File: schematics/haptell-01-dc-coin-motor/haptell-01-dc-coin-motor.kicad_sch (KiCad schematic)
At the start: 5 parts, among them M1 3-5V DC coin motor, Q1 IRF3205

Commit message: Improve KiCad motor driver schematic
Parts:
- removed D1: 1N5819, symbol Device:D_Schottky
- removed M1: 3-5V DC coin motor, symbol Motor:Motor_DC
- removed Q1: IRF3205, symbol Transistor_FET:IRF3205
- removed R1: 220R, symbol Device:R
- removed R2: 10k, symbol Device:R
- added D1: 1N5819, symbol D_Schottky
- added M1: 3-5V DC coin motor, symbol Motor_DC
- added Q1: IRF3205, Package_TO_SOT_THT:TO-220-3_Vertical, symbol Q_NMOS
- added R1: 220R, symbol R
- added R2: 10k, symbol R
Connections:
- net GND: now also Q1.S, R2.2
- new net: Q1.G, R2.1
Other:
- note added: "Arduino UNO R4 WiFi pins"
- note added: "D1 flyback diode: cathode / marked end to +5V, anode to drain node."
- note added: "D9 PWM drives only the MOSFET gate. Motor current flows through Q1."
- note added: "Motor driver stage"
- note added: "common ground"
- note added: "drain node: motor - / diode anode / Q1 drain"
- note added: "gate pulldown"
- note added: "haptell-01 DC coin vibration motor driver"
- note removed: "Arduino UNO R4 WiFi connections: D9 PWM -> R1 -> MOSFET gate 5V -> motor positive GND -> MOSFET source and pulldown"
- note removed: "D1 cathode / marked end to 5V. D1 anode to MOSFET drain."
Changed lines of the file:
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@@
     (title "haptell-01 DC Coin Motor Driver")
     (date "2026-05-12")
-    (rev "0.1")
+    (rev "0.2")
     (company "Haptell")
     (comment 1 "Arduino UNO R4 WiFi low-side MOSFET motor driver")
   )
-  (junction (at 88.9 58.42) (diameter 0) (color 0 0 0 0)
+  (text "haptell-01 DC coin vibration motor driver" (at 25.4 25.4 0)
+    (effects (font (size 3.048 3.048) (bold yes)) (justify left bottom))
   )
-  (junction (at 88.9 109.22) (diameter 0) (color 0 0 0 0)
+  (text "D9 PWM drives only the MOSFET gate. Motor current flows through Q1." (at 25.4 31.75 0)
+    (effects (font (size 1.778 1.778)) (justify left bottom))
   )
-  (junction (at 139.7 76.2) (diameter 0) (color 0 0 0 0)
+  (text "D1 flyback diode: cathode / marked end to +5V, anode to drain node." (at 25.4 36.83 0)
+    (effects (font (size 1.778 1.778)) (justify left bottom))
   )
-  (wire (pts (xy 25.4 58.42) (xy 45.72 58.42))
-    (stroke (width 0) (type default))
+  (text "Arduino UNO R4 WiFi pins" (at 25.4 43.18 0)
+    (effects (font (size 1.778 1.778) (bold yes)) (justify left bottom))
   )
-  (wire (pts (xy 66.04 58.42) (xy 88.9 58.42))
-    (stroke (width 0) (type default))
+  (text "Motor driver stage" (at 101.6 43.18 0)
+    (effects (font (size 1.778 1.778) (bold yes)) (justify left bottom))
   )
-  (wire (pts (xy 88.9 58.42) (xy 88.9 76.2))
-    (stroke (width 0) (type default))
-  )
-  (wire (pts (xy 88.9 58.42) (xy 114.3 58.42))
-    (stroke (width 0) (type default))
-  )
-  (wire (pts (xy 25.4 76.2) (xy 114.3 76.2))
-    (stroke (width 0) (type default))
-  )
-  (wire (pts (xy 134.62 76.2) (xy 139.7 76.2))
-    (stroke (width 0) (type default))
-  )
-  (wire (pts (xy 139.7 76.2) (xy 139.7 88.9))
-    (stroke (width 0) (type default))
-  )
-  (wire (pts (xy 139.7 76.2) (xy 157.48 76.2))
-    (stroke (width 0) (type default))
-  )
-  (wire (pts (xy 88.9 96.52) (xy 88.9 109.22))
-    (stroke (width 0) (type default))
-  )
-  (wire (pts (xy 25.4 109.22) (xy 88.9 109.22))
-    (stroke (width 0) (type default))
-  )
-  (wire (pts (xy 88.9 109.22) (xy 139.7 109.22))
-    (stroke (width 0) (type default))
-  )
-  (wire (pts (xy 139.7 99.06) (xy 139.7 109.22))
-    (stroke (width 0) (type default))
-  )
-  (text "Arduino UNO R4 WiFi connections:\nD9 PWM -> R1 -> MOSFET gate\n5V -> motor positive\nGND -> MOSFET source and pulldown" (at 24.13 30.48 0)
-    (effects (font (size 3.048 3.048)) (justify left bottom))
-  )
-  (text "D1 cathode / marked end to 5V.\nD1 anode to MOSFET drain." (at 104.14 43.18 0)
-    (effects (font (size 2.54 2.54)) (justify left bottom))
-  )
-  (global_label "D9_PWM" (shape input) (at 25.4 58.42 180)
+  (global_label "D9_PWM" (shape input) (at 25.4 88.9 180)
     (effects (font (size 1.27 1.27)) (justify right))
   )
-  (global_label "+5V" (shape passive) (at 25.4 76.2 180)
+  (global_label "+5V" (shape passive) (at 25.4 55.88 180)
     (effects (font (size 1.27 1.27)) (justify right))
   )
-  (global_label "GND" (shape passive) (at 25.4 109.22 180)
+  (global_label "GND" (shape passive) (at 25.4 127 180)
     (effects (font (size 1.27 1.27)) (justify right))
   )
-  (symbol (lib_id "Device:R") (at 55.88 58.42 90) (unit 1)
+  (junction (at 81.28 88.9) (diameter 0) (color 0 0 0 0))
+  (junction (at 81.28 127) (diameter 0) (color 0 0 0 0))
+  (junction (at 111.76 55.88) (diameter 0) (color 0 0 0 0))
+  (junction (at 139.7 78.74) (diameter 0) (color 0 0 0 0))
+  (junction (at 142.24 127) (diameter 0) (color 0 0 0 0))
+  (wire (pts (xy 25.4 88.9) (xy 48.26 88.9)) (stroke (width 0) (type default)))
+  (wire (pts (xy 58.42 88.9) (xy 81.28 88.9)) (stroke (width 0) (type default)))
+  (wire (pts (xy 81.28 88.9) (xy 99.06 88.9)) (stroke (width 0) (type default)))
+  (wire (pts (xy 99.06 88.9) (xy 99.06 109.22)) (stroke (width 0) (type default)))
+  (wire (pts (xy 99.06 109.22) (xy 134.62 109.22)) (stroke (width 0) (type default)))
+  (wire (pts (xy 81.28 88.9) (xy 81.28 101.6)) (stroke (width 0) (type default)))
+  (wire (pts (xy 81.28 109.22) (xy 81.28 127)) (stroke (width 0) (type default)))
+  (wire (pts (xy 25.4 55.88) (xy 111.76 55.88)) (stroke (width 0) (type default)))
+  (wire (pts (xy 111.76 55.88) (xy 124.46 55.88)) (stroke (width 0) (type default)))
+  (wire (pts (xy 111.76 55.88) (xy 111.76 68.58)) (stroke (width 0) (type default)))
+  (wire (pts (xy 111.76 68.58) (xy 124.46 68.58)) (stroke (width 0) (type default)))
+  (wire (pts (xy 124.46 78.74) (xy 139.7 78.74)) (stroke (width 0) (type default)))
+  (wire (pts (xy 139.7 78.74) (xy 142.24 78.74)) (stroke (width 0) (type default)))
+  (wire (pts (xy 142.24 78.74) (xy 142.24 104.14)) (stroke (width 0) (type default)))
+  (wire (pts (xy 142.24 114.3) (xy 142.24 127)) (stroke (width 0) (type default)))
+  (wire (pts (xy 142.24 127) (xy 25.4 127)) (stroke (width 0) (type default)))
+  (text "gate pulldown" (at 64.77 112.395 0)
+    (effects (font (size 1.27 1.27)) (justify left bottom))
+  )
+  (text "drain node: motor - / diode anode / Q1 drain" (at 142.24 80.01 0)
+    (effects (font (size 1.27 1.27)) (justify left bottom))
+  )
+  (text "common ground" (at 142.24 127 0)
+    (effects (font (size 1.27 1.27)) (justify left bottom))
+  )
+  (symbol (lib_id "R") (at 53.34 88.9 90) (unit 1)
     (in_bom yes) (on_board yes)
-    (property "Reference" "R1" (at 55.88 53.34 90)
-      (effects (font (size 1.27 1.27)))
-    )
-    (property "Value" "220R" (at 55.88 63.5 90)
-      (effects (font (size 1.27 1.27)))
-    )
-    (property "Footprint" "" (at 55.88 58.42 0)
-      (effects (font (size 1.27 1.27)) hide)
-    )
+    (property "Reference" "R1" (at 53.34 83.82 90) (effects (font (size 1.27 1.27))))
+    (property "Value" "220R" (at 53.34 93.98 90) (effects (font (size 1.27 1.27))))
+    (property "Footprint" "" (at 53.34 88.9 0) (effects (font (size 1.27 1.27)) hide))
+    (property "Datasheet" "" (at 53.34 88.9 0) (effects (font (size 1.27 1.27)) hide))
     (pin "1")
     (pin "2")
   )
-  (symbol (lib_id "Device:R") (at 88.9 86.36 0) (unit 1)
+  (symbol (lib_id "R") (at 81.28 105.41 0) (unit 1)
     (in_bom yes) (on_board yes)
-    (property "Reference" "R2" (at 93.98 83.82 0)
-      (effects (font (size 1.27 1.27)))
-    )
-    (property "Value" "10k" (at 93.98 88.9 0)
-      (effects (font (size 1.27 1.27)))
-    )
-    (property "Footprint" "" (at 88.9 86.36 0)
-      (effects (font (size 1.27 1.27)) hide)
-    )
+    (property "Reference" "R2" (at 86.36 102.87 0) (effects (font (size 1.27 1.27))))
+    (property "Value" "10k" (at 86.36 107.95 0) (effects (font (size 1.27 1.27))))
+    (property "Footprint" "" (at 81.28 105.41 0) (effects (font (size 1.27 1.27)) hide))
+    (property "Datasheet" "" (at 81.28 105.41 0) (effects (font (size 1.27 1.27)) hide))
     (pin "1")
     (pin "2")
   )
-  (symbol (lib_id "Motor:Motor_DC") (at 124.46 76.2 90) (unit 1)
+  (symbol (lib_id "Motor_DC") (at 124.46 63.5 0) (unit 1)
     (in_bom yes) (on_board yes)
-    (property "Reference" "M1" (at 124.46 68.58 90)
-      (effects (font (size 1.27 1.27)))
-    )
-    (property "Value" "3-5V DC coin motor" (at 124.46 83.82 90)
-      (effects (font (size 1.27 1.27)))
-    )
-    (property "Footprint" "" (at 124.46 76.2 0)
-      (effects (font (size 1.27 1.27)) hide)
-    )
+    (property "Reference" "M1" (at 128.27 55.88 0) (effects (font (size 1.27 1.27))))
+    (property "Value" "3-5V DC coin motor" (at 128.27 71.12 0) (effects (font (size 1.27 1.27))))
+    (property "Footprint" "" (at 124.46 63.5 0) (effects (font (size 1.27 1.27)) hide))
+    (property "Datasheet" "" (at 124.46 63.5 0) (effects (font (size 1.27 1.27)) hide))
     (pin "1")
     (pin "2")
   )
-  (symbol (lib_id "Device:D_Schottky") (at 124.46 58.42 90) (unit 1)
+  (symbol (lib_id "D_Schottky") (at 111.76 73.66 90) (unit 1)
     (in_bom yes) (on_board yes)
-    (property "Reference" "D1" (at 124.46 50.8 90)
-      (effects (font (size 1.27 1.27)))
-    )
-    (property "Value" "1N5819" (at 124.46 66.04 90)
-      (effects (font (size 1.27 1.27)))
-    )
-    (property "Footprint" "" (at 124.46 58.42 0)
-      (effects (font (size 1.27 1.27)) hide)
-    )
+    (property "Reference" "D1" (at 106.68 73.66 90) (effects (font (size 1.27 1.27))))
+    (property "Value" "1N5819" (at 116.84 73.66 90) (effects (font (size 1.27 1.27))))
+    (property "Footprint" "" (at 111.76 73.66 0) (effects (font (size 1.27 1.27)) hide))
+    (property "Datasheet" "" (at 111.76 73.66 0) (effects (font (size 1.27 1.27)) hide))
     (pin "1")
     (pin "2")
   )
-  (symbol (lib_id "Transistor_FET:IRF3205") (at 139.7 93.98 0) (unit 1)
+  (symbol (lib_id "Q_NMOS") (at 139.7 109.22 0) (unit 1)
     (in_bom yes) (on_board yes)
-    (property "Reference" "Q1" (at 146.05 91.44 0)
-      (effects (font (size 1.27 1.27)))
-    )
-    (property "Value" "IRF3205" (at 147.32 96.52 0)
-      (effects (font (size 1.27 1.27)))
-    )
-    (property "Footprint" "" (at 144.78 101.6 0)
-      (effects (font (size 1.27 1.27)) hide)
-    )
+    (property "Reference" "Q1" (at 146.05 105.41 0) (effects (font (size 1.27 1.27))))
+    (property "Value" "IRF3205" (at 146.05 110.49 0) (effects (font (size 1.27 1.27))))
+    (property "Footprint" "Package_TO_SOT_THT:TO-220-3_Vertical" (at 144.78 111.76 0) (effects (font (size 1.27 1.27)) hide))
+    (property "Datasheet" "http://www.irf.com/product-info/datasheets/data/irf3205.pdf" (at 139.7 109.22 0) (effects (font (size 1.27 1.27)) hide))
     (pin "G")
     (pin "D")

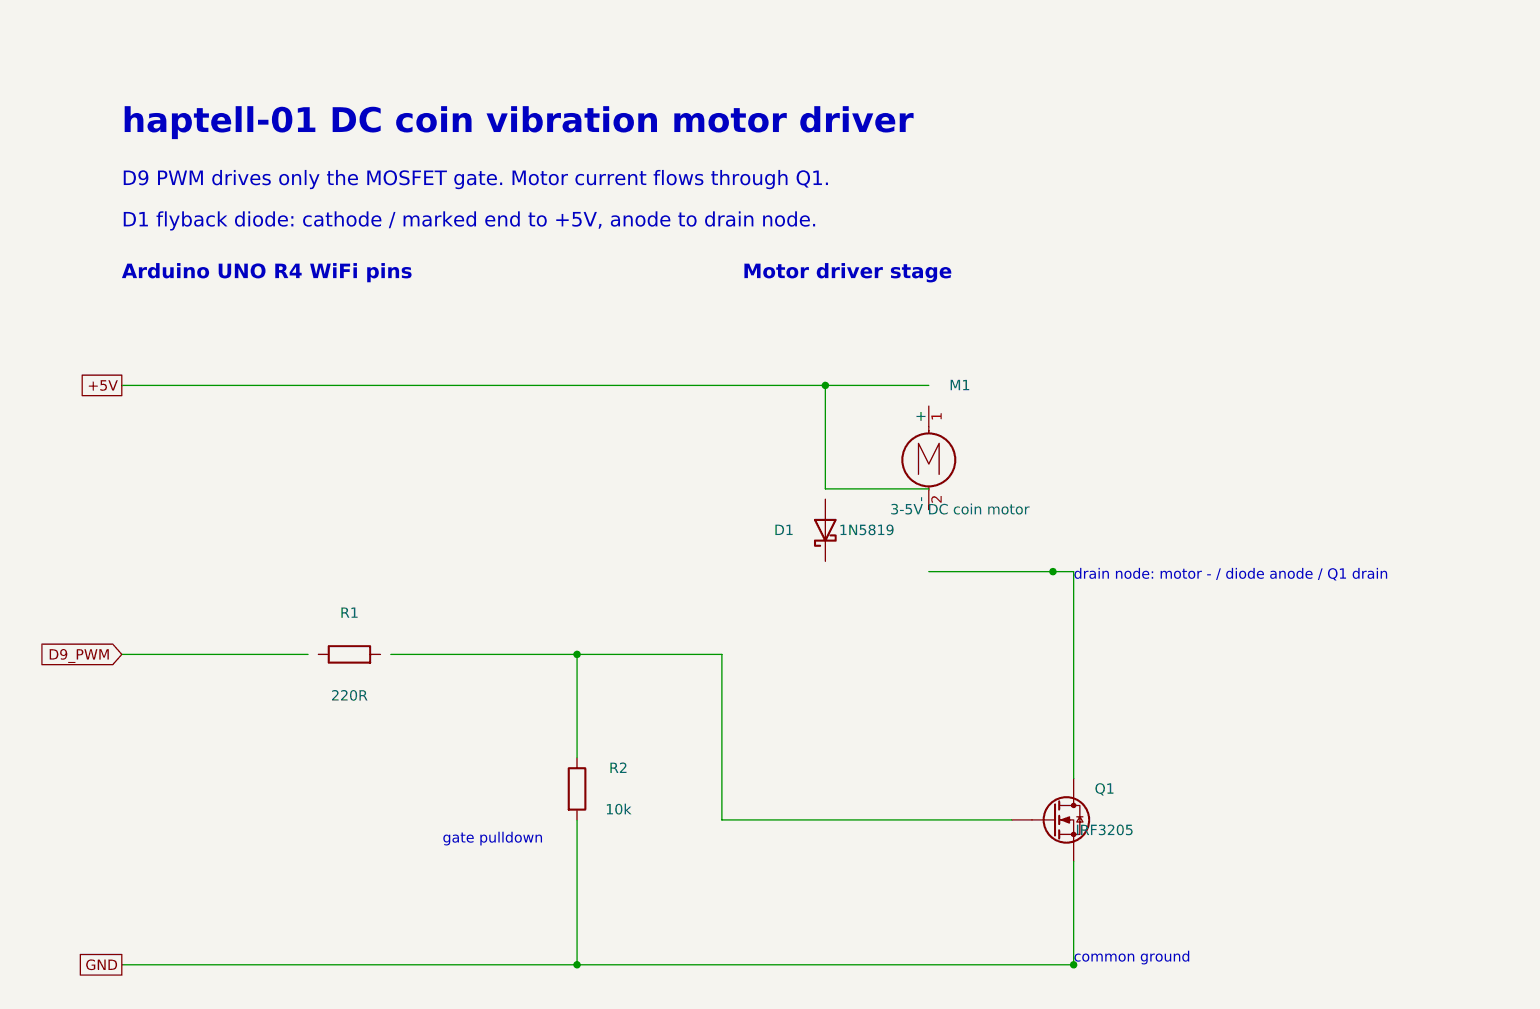
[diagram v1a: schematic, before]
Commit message: Update KiCad schematic layout
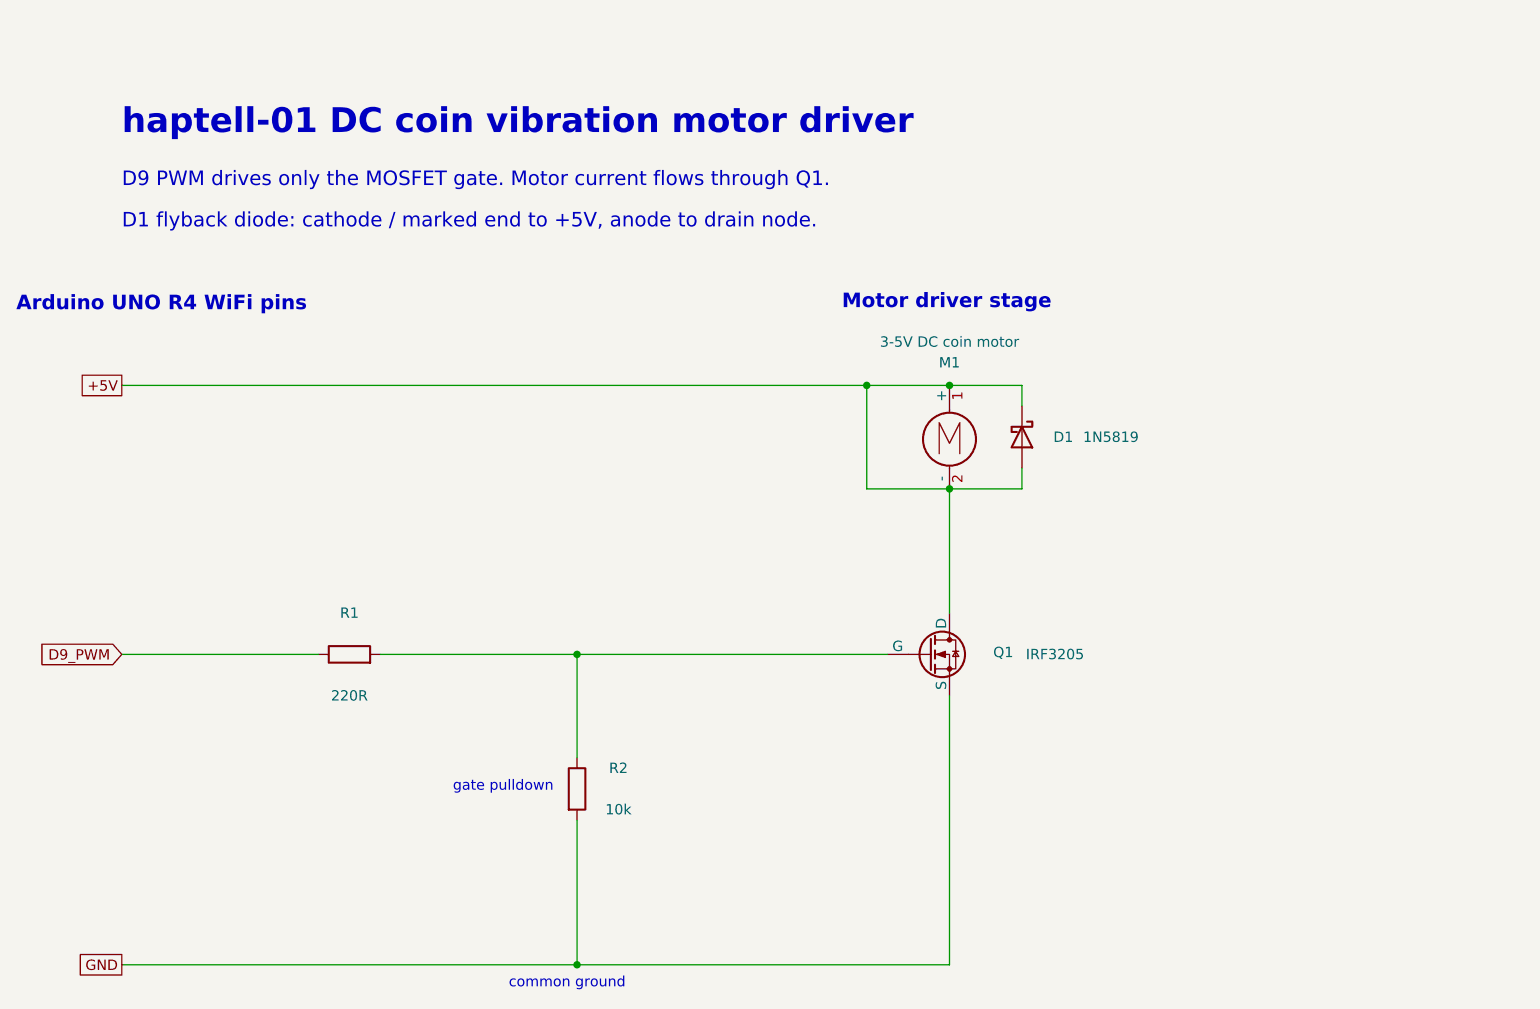
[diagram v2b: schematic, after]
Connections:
- net +5V: now also D1.1 (K), D1.2 (A), M1.1 (+), M1.2 (-), Q1.D
- net D9_PWM: now also R1.1
- net at Q1.G, R2.1: now also R1.2
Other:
- note removed: "drain node: motor - / diode anode / Q1 drain"
- moved on the sheet: D1, M1
